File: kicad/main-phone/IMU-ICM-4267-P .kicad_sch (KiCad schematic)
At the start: 8 parts, among them U19 ICM-42607-P

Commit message: main-phone: free MCU pins; 2x11 spare header with UART and I2C
- LiDAR rail enable joins ~VM-VBAT-EN (PE10); PD9 freed
- IMU FSYNC/INT2 go to J7301 instead of the MCU; FSYNC 100k pull-down (R7601); PD4/PD7 freed
- one open-drain ToF interrupt (PD12) for both VL53L7s and the side VL53L0X; PC8/PE2 freed
- right VL53L7 LPn held up by R7307, no MCU pin; PE8 freed
- IMU moved from I2C2 to I2C4 (R18/R72 not fitted); PA8/PA9 freed;
  R7315 keeps PA9 (UCPD DBCC1) pulled up for dead-battery Rd on CC1
- PWR_EN moved PC10 -> PD7; PC10/PC11 are a spare UART
- J7301 2x6 -> 2x11: 3.3 V, 5 V, I2C4, UART, 12 spare GPIO, IMU FSYNC/INT2, GND
- docs: SPEC, main-phone and side-sensor READMEs

Co-Authored-By: Claude Opus 5.5 <noreply@anthropic.com>
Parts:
- added R7601: 100k, Resistor_SMD:R_0603_1608Metric, symbol Device:R_US
- R18, R72: now not fitted
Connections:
- net GND: now also R7601.2
- net IMU-FSYNC: now also R7601.1
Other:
- note added: "R18/R72: not fitted. The IMU is on I2C4 now (2.2k pull-ups on the MCU sheet)."
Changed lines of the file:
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@@
 		(on_board yes)
 		(in_pos_files yes)
-		(dnp no)
+		(dnp yes)
 		(property "Reference" "R18"
 			(at 103.632 89.916 0)
@@
 		(on_board yes)
 		(in_pos_files yes)
-		(dnp no)
+		(dnp yes)
 		(property "Reference" "R72"
 			(at 112.522 89.916 0)
@@
 		)
 	)
+	(junction
+		(at 120.65 115.57)
+		(diameter 0)
+		(color 0 0 0 0)
+	)
+	(wire
+		(pts
+			(xy 120.65 115.57) (xy 120.65 118.11)
+		)
+		(stroke
+			(width 0)
+			(type default)
+		)
+	)
+	(symbol
+		(lib_id "Device:R_US")
+		(at 120.65 121.92 0)
+		(unit 1)
+		(body_style 1)
+		(exclude_from_sim no)
+		(in_bom yes)
+		(on_board yes)
+		(in_pos_files yes)
+		(dnp no)
+		(property "Reference" "R7601"
+			(at 123.19 120.65 0)
+			(show_name no)
+			(do_not_autoplace no)
+			(effects
+				(font
+					(size 1.27 1.27)
+				)
+				(justify left)
+			)
+		)
+		(property "Value" "100k"
+			(at 123.19 123.19 0)
+			(show_name no)
+			(do_not_autoplace no)
+			(effects
+				(font
+					(size 1.27 1.27)
+				)
+				(justify left)
+			)
+		)
+		(property "Footprint" "Resistor_SMD:R_0603_1608Metric"
+			(at 120.65 121.92 0)
+			(hide yes)
+			(show_name no)
+			(do_not_autoplace no)
+			(effects
+				(font
+					(size 1.27 1.27)
+				)
+			)
+		)
+		(property "Datasheet" ""
+			(at 120.65 121.92 0)
+			(hide yes)
+			(show_name no)
+			(do_not_autoplace no)
+			(effects
+				(font
+					(size 1.27 1.27)
+				)
+			)
+		)
+		(property "Description" "FSYNC pull-down: datasheet says tie FSYNC low when unused; J7301 pin 19 can drive it"
+			(at 120.65 121.92 0)
+			(hide yes)
+			(show_name no)
+			(do_not_autoplace no)
+			(effects
+				(font
+					(size 1.27 1.27)
+				)
+			)
+		)
+		(property "LCSC" "C2907088"
+			(at 120.65 121.92 0)
+			(hide yes)
+			(show_name no)
+			(do_not_autoplace no)
+			(effects
+				(font
+					(size 1.27 1.27)
+				)
+			)
+		)
+		(pin "1"
+		)
+		(pin "2"
+		)
+		(instances
+			(project "Main"
+				(path "/dbcfb655-8d45-4808-9a74-2a0eb03372e8/7b57c0fa-4a35-4109-8672-3c36267bf8ff"
+					(reference "R7601")
+					(unit 1)
+				)
+			)
+		)
+	)
+	(symbol
+		(lib_id "oomwoo-kicad-altium-import:GND_POWER_GROUND")
+		(at 120.65 125.73 0)
+		(unit 1)
+		(body_style 1)
+		(exclude_from_sim no)
+		(in_bom yes)
+		(on_board yes)
+		(in_pos_files yes)
+		(dnp no)
+		(property "Reference" "#PWR07601"
+			(at 120.65 132.08 0)
+			(hide yes)
+			(show_name no)
+			(do_not_autoplace no)
+			(effects
+				(font
+					(size 1.27 1.27)
+				)
+			)
+		)
+		(property "Value" "GND"
+			(at 120.65 132.08 0)
+			(hide yes)
+			(show_name no)
+			(do_not_autoplace no)
+			(effects
+				(font
+					(size 1.27 1.27)
+				)
+			)
+		)
+		(property "Footprint" ""
+			(at 120.65 125.73 0)
+			(hide yes)
+			(show_name no)
+			(do_not_autoplace no)
+			(effects
+				(font
+					(size 1.27 1.27)
+				)
+			)
+		)
+		(property "Datasheet" ""
+			(at 120.65 125.73 0)
+			(hide yes)
+			(show_name no)
+			(do_not_autoplace no)
+			(effects
+				(font
+					(size 1.27 1.27)
+				)
+			)
+		)
+		(property "Description" ""
+			(at 120.65 125.73 0)
+			(hide yes)
+			(show_name no)
+			(do_not_autoplace no)
+			(effects
+				(font
+					(size 1.27 1.27)
+				)
+			)
+		)
+		(pin ""
+		)
+		(instances
+			(project "Main"
+				(path "/dbcfb655-8d45-4808-9a74-2a0eb03372e8/7b57c0fa-4a35-4109-8672-3c36267bf8ff"
+					(reference "#PWR07601")
+					(unit 1)
+				)
+			)
+		)
+	)
+	(text "R18/R72: not fitted. The IMU is on I2C4 now (2.2k pull-ups on the MCU sheet)."
+		(exclude_from_sim no)
+		(at 125.73 135.89 0)
+		(effects
+			(font
+				(size 1.27 1.27)
+			)
+			(justify left bottom)
+		)
+	)

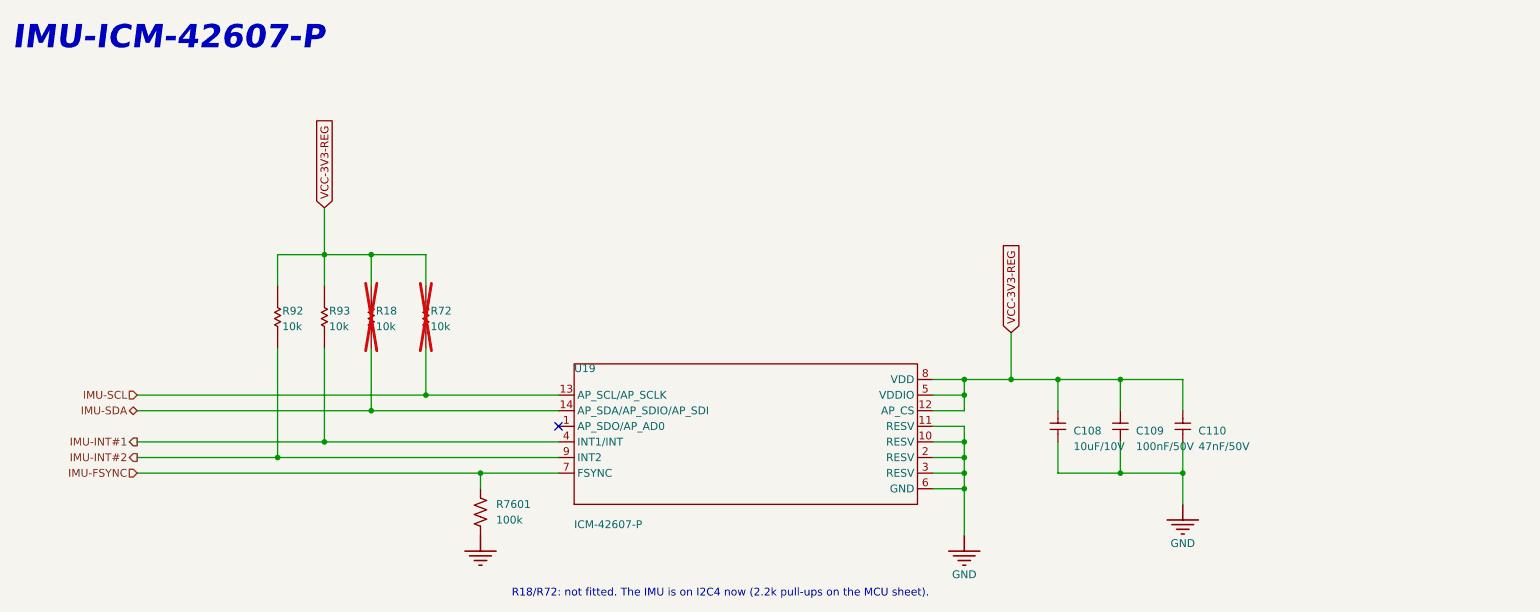
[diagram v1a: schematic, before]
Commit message: Per-board reference ranges, J1 spare header, IMU AD0 pull-down, BOM outputs
- reference ranges: main-phone 1-999, dock 1000s, front ToF 2000s, side 3000s,
  cliff 4000s, rear IR 5000s, Hall 6000s (main-phone 7xxx parts renumbered
  below 1000; sensor boards and dock moved from 8xxx)
- main-phone: J7301 -> J1, a fitted 2x7 0.1" header with spares only
  (3.3 V, 5 V, I2C4, UART PC10/PC11, PA8-PA10, PD4, PE2, PE6, GND)
- IMU: AP_AD0 pulled low by R217 (address 0x68); INT2 on test pad TP1;
  FSYNC reachable on R211; R18/R72 removed
- tools/export.py replaces export_pdfs.py: schematic PDF and JLC-style BOM in
  each board's output/ folder; --pcb adds Gerbers, placement and STEP
- cliff and rear IR projects: fix top-level sheet left over from a copy
- Hall board: visual tidy-up

Co-Authored-By: Claude Opus 5.5 <noreply@anthropic.com>
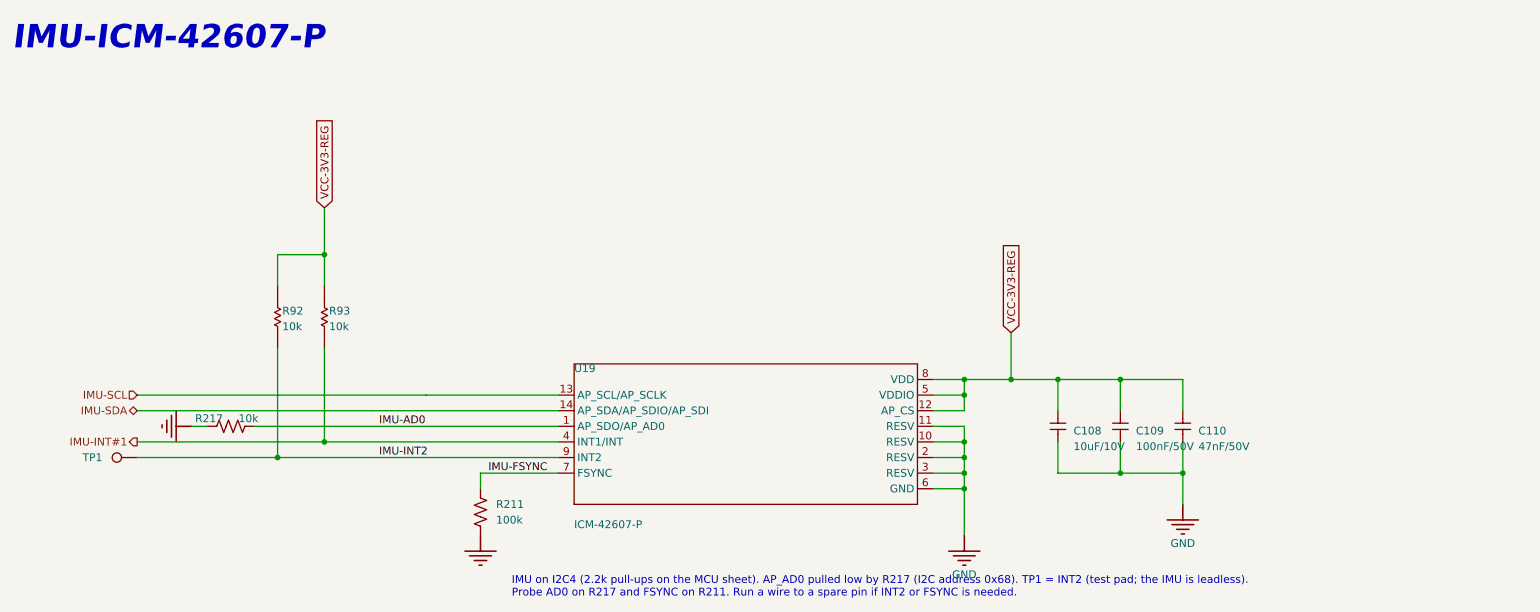
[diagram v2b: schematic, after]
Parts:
- removed R18, R72: 10k, Resistor_SMD:R_0603_1608Metric, symbol DesignLibrary:IMU_3_Resistor-1_DesignLibrary.SchLib
- added R217: 10k, Resistor_SMD:R_0603_1608Metric, symbol Device:R_US
- added TP1: IMU-INT2, TestPoint:TestPoint_Pad_D1.5mm, symbol Connector:TestPoint
- renumbered R7601 to R211
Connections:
- net GND: now also R217.1
- net IMU-AD0: now reaches U19.1 (AP_SDO/AP_AD0)
- net IMU-AD0: now also R217.2
- net IMU-INT#2 renamed IMU-INT2
- net IMU-INT2: now also TP1.1
- no-connect marks 1 -> 0
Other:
- note added: "IMU on I2C4 (2.2k pull-ups on the MCU sheet). AP_AD0 pulled low by R217 (I2C address 0x68). TP1 = INT2 (test pad; the IMU is leadless). Probe AD0 on R217 and FSYNC on R211. Run a wire to a spare pin if INT2 or FSYNC is needed."
- note removed: "R18/R72: not fitted. The IMU is on I2C4 now (2.2k pull-ups on the MCU sheet)."
